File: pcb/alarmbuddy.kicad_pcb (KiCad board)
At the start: 2 copper layers, 81 x 59 mm, 34 parts, among them J1 24VAC, J2 3V3, J3 SENS1-3, J4 SENS4-6, J5 SENS7-9, J6 SENS10-12, J7 eflashy32, U1 BD9G101G, U2 ESP32-S2-WROVER

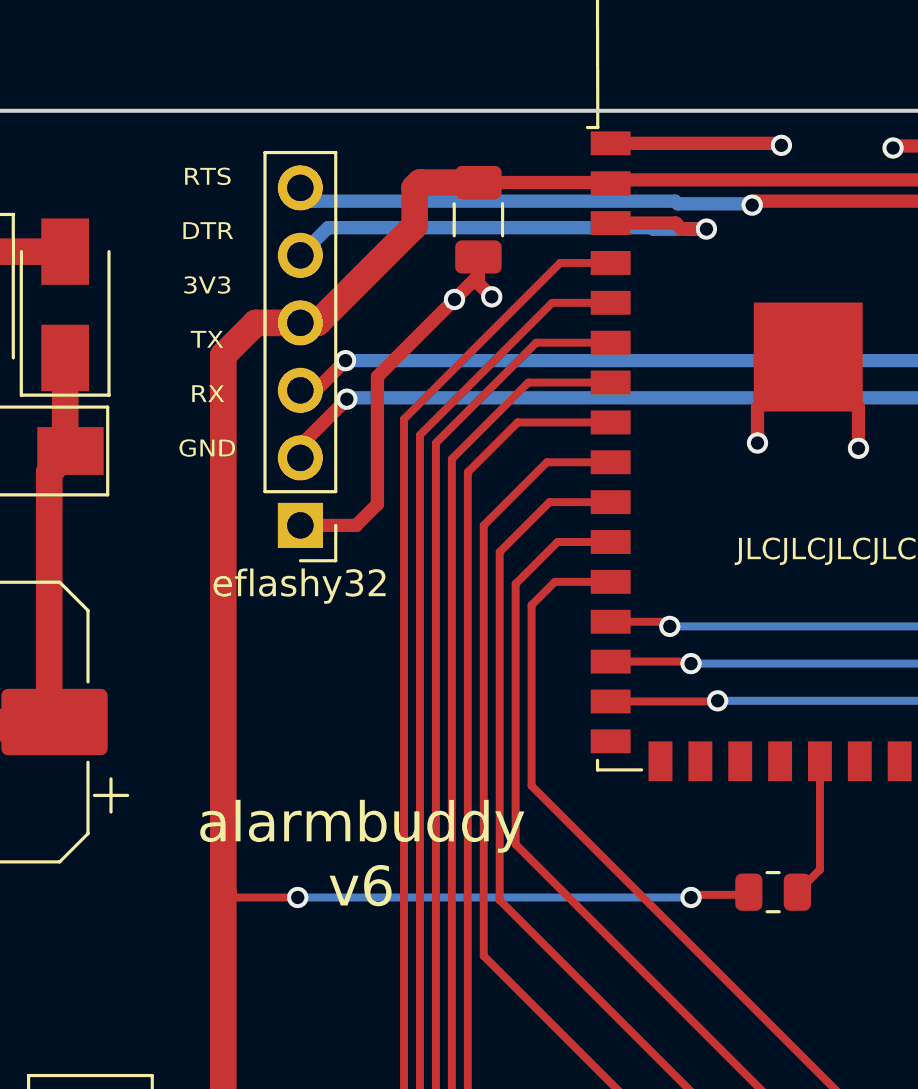
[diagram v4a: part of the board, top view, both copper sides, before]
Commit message: fix programmer mixup with gpio0 :(
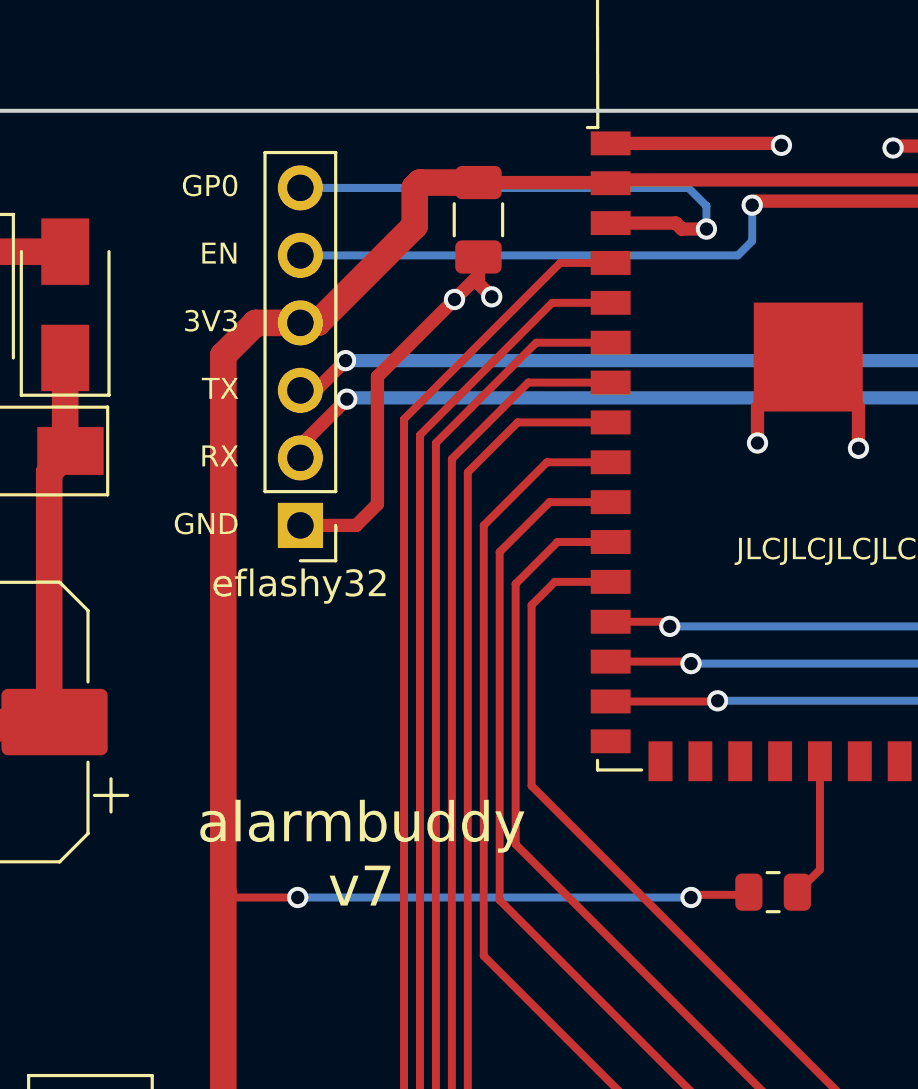
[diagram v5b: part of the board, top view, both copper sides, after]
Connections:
- J7 pad 5: /~{DTR} -> /EN
- J7 pad 6: /RTS -> /GPIO0
- R5 pad 1: /RTS -> /EN
- U2 pad 3: /~{DTR} -> /GPIO0
- U2 pad 41: /RTS -> /EN
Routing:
- net /EN: track 0.00 -> 38.4 mm, vias 0 -> 1
- net /RTS: track 37.1 -> 0.00 mm, vias 1 -> 0
- net /GPIO0: track 0.00 -> 20.1 mm, vias 0 -> 1
- net /~{DTR}: track 19.4 -> 0.00 mm, vias 1 -> 0
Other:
- board text added: "GP0 EN 3V3 TX RX GND"
- board text added: "alarmbuddy v7"
- board text removed: "RTS DTR 3V3 TX RX GND"
- board text removed: "alarmbuddy v6"

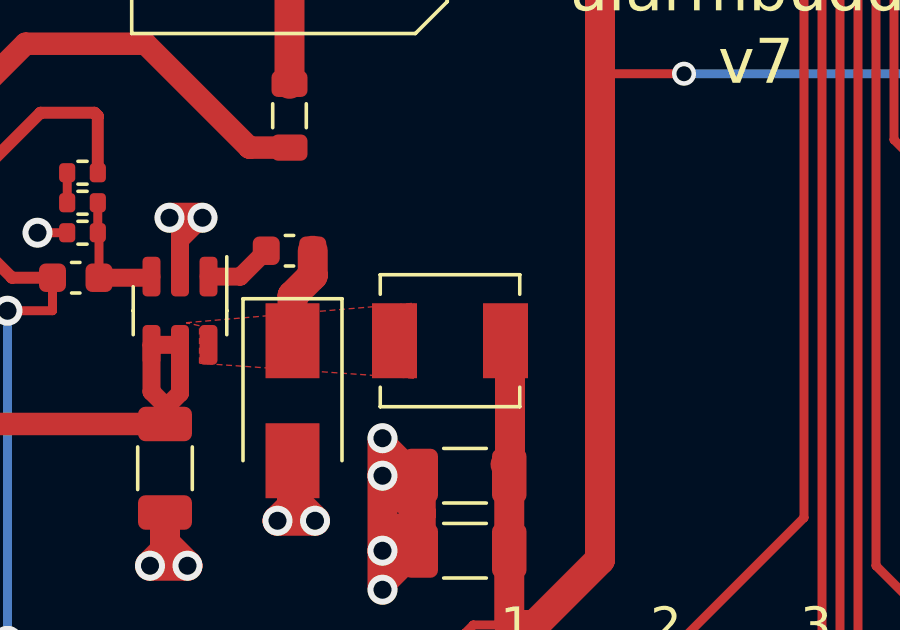
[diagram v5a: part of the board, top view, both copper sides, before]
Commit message: kicad v7 and render
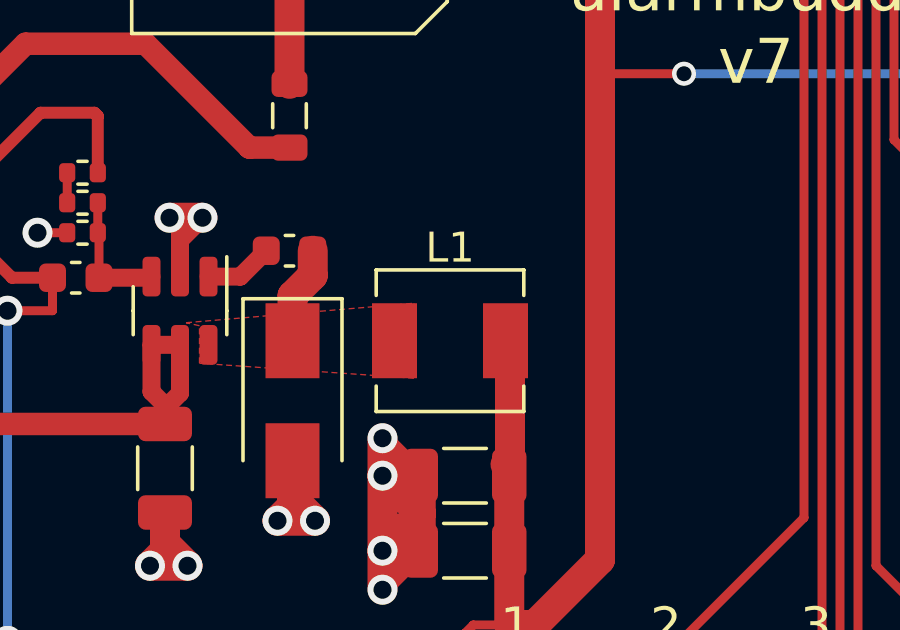
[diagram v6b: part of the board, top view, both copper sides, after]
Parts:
- L1: footprint switching:L_Sunlord_MWSA0402_4.4x4.2mm -> Inductor_SMD:L_Sunlord_MWSA0402S
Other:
- board text removed: "J3"
